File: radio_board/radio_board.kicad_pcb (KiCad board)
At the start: 2 copper layers, 82 x 72.7 mm, 86 parts, among them CN1 HX JN1.27-2X5P ZZ H4.9, Q1 2N7002K, SW2 RKB2SJG250SMTRLFS, SW3 MSK12C02, U1 FSC-BT1036C, U2 TP4057, U3 XB5352A, U4 SKB369, U5 S2B-PH-K-S(LF)(SN), U6 XC6206P332MR

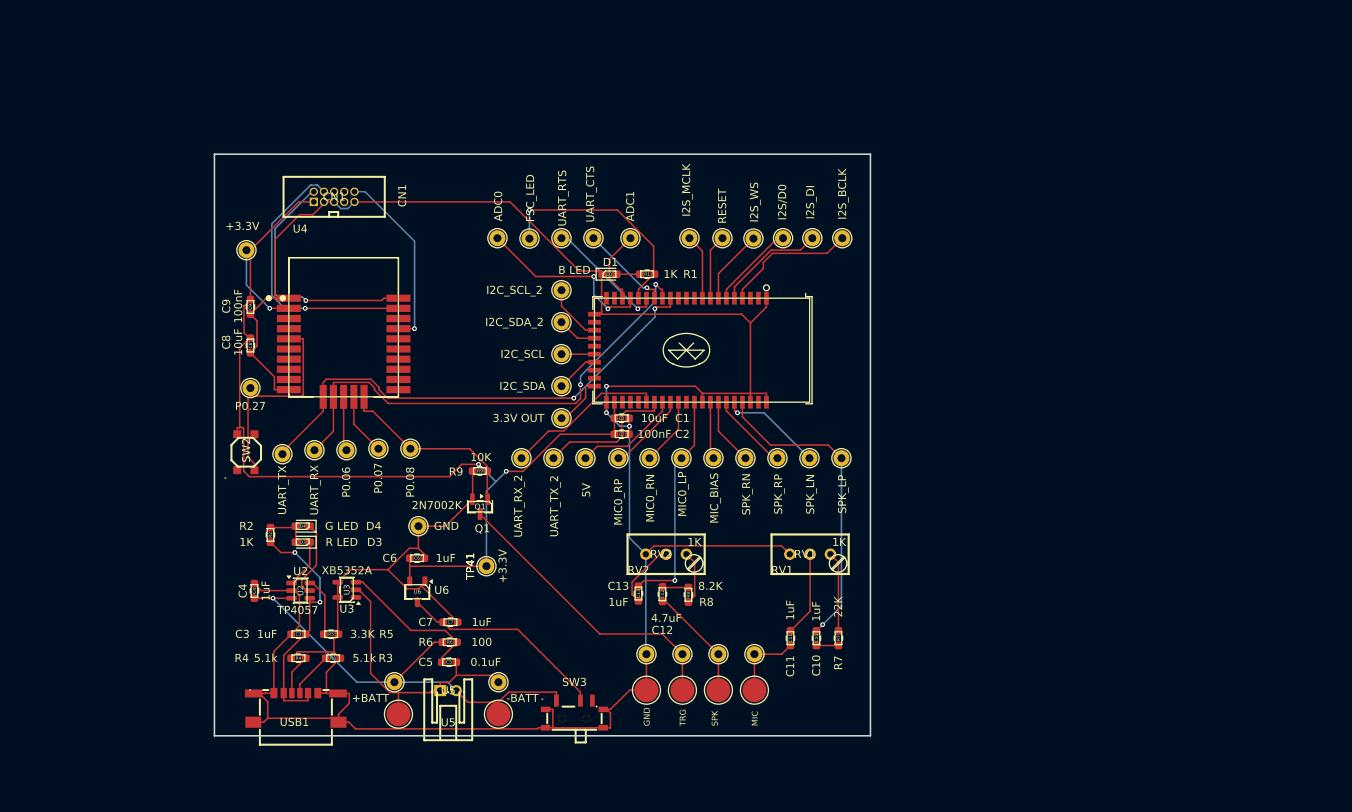
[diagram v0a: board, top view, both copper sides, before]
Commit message: [Housekeeping] Renamed project library
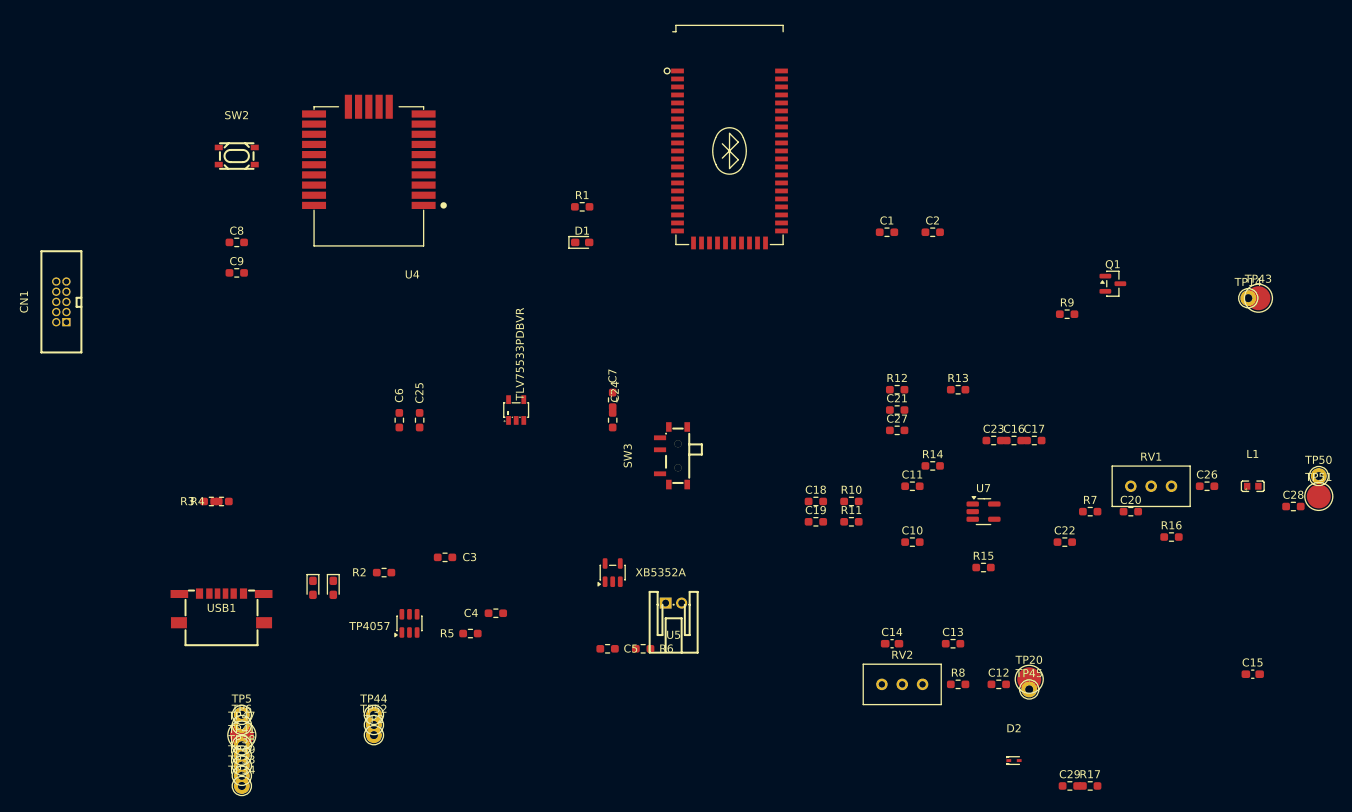
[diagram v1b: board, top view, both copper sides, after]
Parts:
- removed TP1: P0.06, TestPoint:TestPoint_THTPad_D2.0mm_Drill1.0mm
- removed TP10: UART_RX, TestPoint:TestPoint_THTPad_D2.0mm_Drill1.0mm
- removed TP11: UART_RX_2, TestPoint:TestPoint_THTPad_D2.0mm_Drill1.0mm
- removed TP12: UART_TX_2, TestPoint:TestPoint_THTPad_D2.0mm_Drill1.0mm
- removed TP13: MIC_BIAS, TestPoint:TestPoint_THTPad_D2.0mm_Drill1.0mm
- removed TP15: I2C_SCL_2, TestPoint:TestPoint_THTPad_D2.0mm_Drill1.0mm
- removed TP16: I2C_SDA_2, TestPoint:TestPoint_THTPad_D2.0mm_Drill1.0mm
- removed TP17: UART_CTS, TestPoint:TestPoint_THTPad_D2.0mm_Drill1.0mm
- removed TP18: UART_RTS, TestPoint:TestPoint_THTPad_D2.0mm_Drill1.0mm
- removed TP19: FSC_LED, TestPoint:TestPoint_THTPad_D2.0mm_Drill1.0mm
- removed TP21: 5V, TestPoint:TestPoint_THTPad_D2.0mm_Drill1.0mm
- removed TP22: RESET, TestPoint:TestPoint_THTPad_D2.0mm_Drill1.0mm
- removed TP23: I2S_WS, TestPoint:TestPoint_THTPad_D2.0mm_Drill1.0mm
- removed TP24: I2S/D0, TestPoint:TestPoint_THTPad_D2.0mm_Drill1.0mm
- removed TP25: I2S_DI, TestPoint:TestPoint_THTPad_D2.0mm_Drill1.0mm
- removed TP26: I2S_BCLK, TestPoint:TestPoint_THTPad_D2.0mm_Drill1.0mm
- removed TP27: I2S_MCLK, TestPoint:TestPoint_THTPad_D2.0mm_Drill1.0mm
- removed TP28: ADC0, TestPoint:TestPoint_THTPad_D2.0mm_Drill1.0mm
- removed TP29: ADC1, TestPoint:TestPoint_THTPad_D2.0mm_Drill1.0mm
- removed TP3: P0.08, TestPoint:TestPoint_THTPad_D2.0mm_Drill1.0mm
- removed TP30: I2C_SCL, TestPoint:TestPoint_THTPad_D2.0mm_Drill1.0mm
- removed TP31: I2C_SDA, TestPoint:TestPoint_THTPad_D2.0mm_Drill1.0mm
- removed TP32: 3.3V OUT, TestPoint:TestPoint_THTPad_D2.0mm_Drill1.0mm
- removed TP35: SPK_RP, TestPoint:TestPoint_THTPad_D2.0mm_Drill1.0mm
- removed TP36: SPK_RN, TestPoint:TestPoint_THTPad_D2.0mm_Drill1.0mm
- removed TP37: K_CONNECTOR_MIC_IN, TestPoint:TestPoint_Pad_D3.0mm
- removed TP39: MIC0_RN, TestPoint:TestPoint_THTPad_D2.0mm_Drill1.0mm
- removed TP4: P0.27, TestPoint:TestPoint_THTPad_D2.0mm_Drill1.0mm
- removed TP40: MIC0_RP, TestPoint:TestPoint_THTPad_D2.0mm_Drill1.0mm
- removed TP42: GND, TestPoint:TestPoint_THTPad_D2.0mm_Drill1.0mm
- removed TP46: GND, TestPoint:TestPoint_Pad_D3.0mm
- removed TP48: -BATT, TestPoint:TestPoint_Pad_D3.0mm
- removed TP7: +3.3V, TestPoint:TestPoint_THTPad_D2.0mm_Drill1.0mm
- removed TP8: +BATT, TestPoint:TestPoint_THTPad_D2.0mm_Drill1.0mm
- removed TP9: UART_TX, TestPoint:TestPoint_THTPad_D2.0mm_Drill1.0mm
- added C14: 1nF, Capacitor_SMD:C_0603_1608Metric_Pad1.08x0.95mm_HandSolder, F.Cu at (155.2, 117.2)
- added C15: 1uF, Capacitor_SMD:C_0603_1608Metric_Pad1.08x0.95mm_HandSolder, F.Cu at (200.3, 121.0)
- added C16: 100 nF, Resistor_SMD:R_0603_1608Metric_Pad0.98x0.95mm_HandSolder, F.Cu at (170.4, 91.8)
- added C17: 10uF, Resistor_SMD:R_0603_1608Metric_Pad0.98x0.95mm_HandSolder, F.Cu at (173.0, 91.8)
- added C18: 1uF, Resistor_SMD:R_0603_1608Metric_Pad0.98x0.95mm_HandSolder, F.Cu at (145.7, 99.4)
- added C19: 1uF, Resistor_SMD:R_0603_1608Metric_Pad0.98x0.95mm_HandSolder, F.Cu at (145.7, 102.0)
- added C20: 1uF, Resistor_SMD:R_0603_1608Metric_Pad0.98x0.95mm_HandSolder, F.Cu at (185.1, 100.7)
- added C21: 10uF, Resistor_SMD:R_0603_1608Metric_Pad0.98x0.95mm_HandSolder, F.Cu at (155.8, 88.0)
- added C22: 33 pF, Resistor_SMD:R_0603_1608Metric_Pad0.98x0.95mm_HandSolder, F.Cu at (176.8, 104.5)
- added C23: 33 pF, Resistor_SMD:R_0603_1608Metric_Pad0.98x0.95mm_HandSolder, F.Cu at (167.9, 91.8)
- added C24: 100nF, Resistor_SMD:R_0603_1608Metric_Pad0.98x0.95mm_HandSolder, F.Cu at (120.3, 89.2)
- added C25: 100nF, Resistor_SMD:R_0603_1608Metric_Pad0.98x0.95mm_HandSolder, F.Cu at (96.2, 89.2)
- added C26: 1uF, Resistor_SMD:R_0603_1608Metric_Pad0.98x0.95mm_HandSolder, F.Cu at (194.6, 97.5)
- added C27: 100nF, Resistor_SMD:R_0603_1608Metric_Pad0.98x0.95mm_HandSolder, F.Cu at (155.8, 90.5)
- added C28: 1nF, Resistor_SMD:R_0603_1608Metric_Pad0.98x0.95mm_HandSolder, F.Cu at (205.4, 100.0)
- added C29: 100nF, Resistor_SMD:R_0603_1608Metric_Pad0.98x0.95mm_HandSolder, F.Cu at (177.4, 135.0)
- added D2: RB521S-30_C727120, PTT_Project_library:SOD-523_L1.2-W0.8-LS1.6-RD, F.Cu at (170.4, 131.8)
- added L1: BLM18KG601SN1D, PTT_Project_library:L0603, F.Cu at (200.3, 97.5)
- added R10: 47k, Resistor_SMD:R_0603_1608Metric_Pad0.98x0.95mm_HandSolder, F.Cu at (150.1, 99.4)
- added R11: 47k, Resistor_SMD:R_0603_1608Metric_Pad0.98x0.95mm_HandSolder, F.Cu at (150.1, 102.0)
- added R12: 10k, Resistor_SMD:R_0603_1608Metric_Pad0.98x0.95mm_HandSolder, F.Cu at (155.8, 85.4)
- added R13: 10k, Resistor_SMD:R_0603_1608Metric_Pad0.98x0.95mm_HandSolder, F.Cu at (163.5, 85.4)
- added R14: 10k, Resistor_SMD:R_0603_1608Metric_Pad0.98x0.95mm_HandSolder, F.Cu at (160.3, 95.0)
- added R15: 10k, Resistor_SMD:R_0603_1608Metric_Pad0.98x0.95mm_HandSolder, F.Cu at (166.6, 107.7)
- added R16: 100, Resistor_SMD:R_0603_1608Metric_Pad0.98x0.95mm_HandSolder, F.Cu at (190.1, 103.9)
- added R17: 470k, Resistor_SMD:R_0603_1608Metric_Pad0.98x0.95mm_HandSolder, F.Cu at (180.0, 135.0)
- added TP49: MIC0_LN, TestPoint:TestPoint_THTPad_D2.0mm_Drill1.0mm, F.Cu at (73.9, 132.4)
- added TP50: K_CONNECTOR_MIC_IN, TestPoint:TestPoint_THTPad_D2.0mm_Drill1.0mm, F.Cu at (208.5, 96.2)
- added TP51: K_CONNECTOR_MIC_IN, TestPoint:TestPoint_Pad_D3.0mm, F.Cu at (208.5, 98.8)
- added TP52: P0.31, TestPoint:TestPoint_THTPad_D2.0mm_Drill1.0mm, F.Cu at (90.4, 127.3)
- added U7: LMV321, Package_TO_SOT_SMD:SOT-23-5_HandSoldering, F.Cu at (166.6, 100.7)
- C10, C11: value 1uF -> 33 pF
- C6, C7: value 1uF -> 10uF
- CN1: footprint PTT_project:CONN-TH_10P-P1.27_HX-JN1.27-2X5P-ZZ-H4.9 -> PTT_Project_library:CONN-TH_10P-P1.27_HX-JN1.27-2X5P-ZZ-H4.9
- R7: value 22K -> 4.7k
- SW2: footprint PTT_project:Push button C2927788 -> PTT_Project_library:SW-SMD_4P-L4.2-W3.2-P2.15-LS4.6
- SW3: footprint PTT_project:SW-TH_MSK12C02 -> PTT_Project_library:SW-TH_MSK12C02
- TP2: value P0.07 -> P0.08
- TP44: value K_CONNECTOR_MIC_IN -> P0.30
- U1: footprint PTT_project:FSC-BT1036C -> PTT_Project_library:FSC-BT1036C
- U4: footprint PTT_project:SKYLAB_SKB369 -> PTT_Project_library:SKYLAB_SKB369
- U5: footprint PTT_project:CONN-TH_S2B-PH-K-S-LF-SN -> PTT_Project_library:CONN-TH_S2B-PH-K-S-LF-SN
- U6: value XC6206P332MR -> TLV75533PDBVR; footprint Package_TO_SOT_SMD:TSOT-23 -> PTT_Project_library:SOT-23-5_L3.0-W1.7-P0.95-LS2.8-BR
- USB1: footprint PTT_project:USB-C-SMD_TYPE-C-6P-QT073 -> PTT_Project_library:USB-C-SMD_TYPE-C-6P-QT073
- moved TP43 87.1 mm to (201.0, 74.0), turned to 0 degrees
- moved TP33 84.8 mm to (73.9, 133.7), turned to 0 degrees
- moved Q1 83.9 mm to (182.8, 72.2), turned to 0 degrees
- moved TP14 83.6 mm to (199.7, 74.0)
- moved TP34 81.9 mm to (73.9, 135.0), turned to 0 degrees
- moved R9 76.0 mm to (177.1, 76.0), turned to 0 degrees
- moved TP38 66.3 mm to (73.9, 131.2), turned to 0 degrees
- moved TP5 51.1 mm to (73.9, 126.1), turned to 0 degrees
- moved TP44 48.2 mm to (90.4, 126.1)
- moved C2 46.4 mm to (160.3, 65.8), turned to 0 degrees
- moved C12 43.5 mm to (168.5, 122.3), turned to 0 degrees
- moved RV1 43.5 mm to (190.1, 97.5)
- moved C1 40.5 mm to (154.6, 65.8), turned to 0 degrees
- moved C13 39.8 mm to (162.8, 117.2), turned to 0 degrees
- moved TP45 39.1 mm to (172.3, 122.9)
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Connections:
- C1 pad 1: GND -> +3.3V
- C10 pad 1: SPK_LP -> Net-(U7--)
- C10 pad 2: Net-(C10-Pad2) -> +3.3V
- C11 pad 1: Net-(C11-Pad1) -> Net-(U7-+)
- C11 pad 2: Net-(C11-Pad2) -> +3.3V
- C13 pad 1: MIC0_LP -> Net-(C13-Pad1)
- C13 pad 2: Net-(C13-Pad2) -> MIC0_LP
- C2 pad 1: GND -> +3.3V
- C3 pad 1: GND -> +3.3V
- C4 pad 2: GND -> +3.3V
- C6 pad 2: GND -> +3.3V
- C7 pad 1: GND -> +3.3V
- C7 pad 2: Net-(U6-VIN) -> Net-(U6-EN)
- C8 pad 1: GND -> +3.3V
- C9 pad 1: GND -> +3.3V
- CN1 pad 3: GND -> +3.3V
- CN1 pad 5: GND -> +3.3V
- CN1 pad 9: GND -> +3.3V
- D1 pad 1: GND -> +3.3V
- Q1 pad 2: GND -> +3.3V
- R3 pad 1: GND -> +3.3V
- R4 pad 1: GND -> +3.3V
- R5 pad 2: GND -> +3.3V
- R7 pad 1: Net-(C10-Pad2) -> Net-(C22-Pad2)
- R7 pad 2: Net-(R7-Pad2) -> Net-(C20-Pad1)
- R9 pad 2: GND -> +3.3V
- RV1 pad 1: Net-(R7-Pad2) -> unconnected-(RV1-Pad1)
- RV1 pad 2: Net-(C11-Pad2) -> Net-(C26-Pad1)
- RV1 pad 3: GND -> Net-(C20-Pad2)
- RV2 pad 2: Net-(C13-Pad2) -> Net-(C13-Pad1)
- RV2 pad 3: GND -> +3.3V
- SW3 pad 2: Net-(U6-VIN) -> unconnected-(SW3-Pad2)
- SW3 pad 4: GND -> +3.3V
- TP2 pad 1: Net-(U4-P0.07) -> P0.08
- TP44 pad 1: Net-(C11-Pad1) -> P0.30
- TP5 pad 1: GND -> +3.3V
- U1 pad 1: GND -> +3.3V
- U1 pad 15: Net-(U1-P4/UART_CTS) -> unconnected-(U1-P4/UART_CTS-Pad15)
- U1 pad 16: Net-(U1-P5/UART_RTS) -> unconnected-(U1-P5/UART_RTS-Pad16)
- U1 pad 18: Net-(U1-P11/ADC0) -> unconnected-(U1-P11/ADC0-Pad18)
- U1 pad 19: Net-(TP29-Pad1) -> unconnected-(U1-P37/ADC1-Pad19)
- U1 pad 22: GND -> +3.3V
- U1 pad 24: Net-(TP15-Pad1) -> unconnected-(U1-P38/I2C_SCL-Pad24)
- U1 pad 25: Net-(TP16-Pad1) -> unconnected-(U1-P39/I2C_SDA-Pad25)
- U1 pad 27: Net-(TP30-Pad1) -> unconnected-(U1-P38/I2C_SCL-Pad27)
- U1 pad 28: Net-(TP31-Pad1) -> unconnected-(U1-P39/I2C_SDA-Pad28)
- U1 pad 31: Net-(U1-3.3V_OUT) -> unconnected-(U1-3.3V_OUT-Pad31)
- U1 pad 32: GND -> +3.3V
- U1 pad 37: Net-(TP11-Pad1) -> unconnected-(U1-P1/UART_RX/DP-Pad37)
- U1 pad 38: Net-(TP12-Pad1) -> unconnected-(U1-P0/UART_TX/DN-Pad38)
- U1 pad 39: Net-(U1-+5V) -> unconnected-(U1-+5V-Pad39)
- U1 pad 4: Net-(U1-P30/I2S_BCLK) -> unconnected-(U1-P30/I2S_BCLK-Pad4)
- U1 pad 44: GND -> MIC0_LN
- U1 pad 5: Net-(U1-P32/I2S_DI) -> unconnected-(U1-P32/I2S_DI-Pad5)
- U1 pad 50: GND -> +3.3V
- U1 pad 52: GND -> +3.3V
- U1 pad 6: Net-(U1-P33//I2S_DO) -> unconnected-(U1-P33//I2S_DO-Pad6)
- U1 pad 7: Net-(U1-P31/I2S_WS) -> unconnected-(U1-P31/I2S_WS-Pad7)
- U1 pad 8: Net-(U1-RESET) -> RESET_FSC
- U1 pad 9: Net-(U1-I2S_MCLK) -> unconnected-(U1-I2S_MCLK-Pad9)
- U2 pad 2: GND -> +3.3V
- U3 pad 4: GND -> +3.3V
- U3 pad 5: GND -> +3.3V
- U4 pad 1: GND -> +3.3V
- U4 pad 10: GND -> +3.3V
- U4 pad 13: Net-(U4-P0.06) -> unconnected-(U4-P0.06-Pad13)
- U4 pad 14: Net-(U4-P0.07) -> unconnected-(U4-P0.07-Pad14)
- U4 pad 22: RESET -> RESET_SKB
- U4 pad 8: unconnected-(U4-P0.30-Pad8) -> P0.30
- U4 pad 9: unconnected-(U4-P0.31-Pad9) -> P0.31
- U6 pad 1: GND -> Net-(U6-EN)
- U6 pad 3: Net-(U6-VIN) -> Net-(U6-EN)
- USB1 pad 7: GND -> +3.3V
- USB1 pad A12: GND -> +3.3V
- USB1 pad B12: GND -> +3.3V
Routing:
- net GND: track 350.4 -> 0.00 mm, vias 3 -> 0
- net +3.3V: track 130.3 -> 0.00 mm, vias 3 -> 0
- net UART_TX: track 62.2 -> 0.00 mm, vias 2 -> 0
- net UART_RX: track 62.2 -> 0.00 mm, vias 2 -> 0
- net +BATT: track 56.6 -> 0.00 mm, vias 1 -> 0
- net SPK_LP: track 39.2 -> 0.00 mm, vias 1 -> 0
- net Net-(Q1-D): track 37.0 -> 0.00 mm
- net -BATT: track 34.6 -> 0.00 mm
- net SWDCLK: track 34.3 -> 0.00 mm, vias 1 -> 0
- net SWDIO: track 30.8 -> 0.00 mm, vias 1 -> 0
- net 5V_usb: track 30.6 -> 0.00 mm, vias 2 -> 0
- net FSC_LED: track 28.4 -> 0.00 mm, vias 1 -> 0
- net MIC0_LP: track 28.2 -> 0.00 mm, vias 1 -> 0
- net Net-(U4-P0.27): track 26.2 -> 0.00 mm
- net Net-(U6-VIN): track 26.1 -> 0.00 mm
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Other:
- board outline removed
- board text removed: "GND"
- board text removed: "MIC"
- board text removed: "SPK"
- board text removed: "TRG"

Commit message: [WIP]
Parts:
- removed U4: SKB369, PTT_Project_library:SKYLAB_SKB369
- added C30: 100nF, Resistor_SMD:R_0603_1608Metric_Pad0.98x0.95mm_HandSolder, F.Cu at (70.8, 60.2)
- added C31: 100nF, Resistor_SMD:R_0603_1608Metric_Pad0.98x0.95mm_HandSolder, F.Cu at (123.0, 47.5)
- added D5: B LED, LED_SMD:LED_0603_1608Metric_Pad1.05x0.95mm_HandSolder, F.Cu at (73.9, 71.0)
- added R18: 10K, Resistor_SMD:R_0603_1608Metric_Pad0.98x0.95mm_HandSolder, F.Cu at (93.0, 54.0)
- added R19: 1K, Resistor_SMD:R_0603_1608Metric_Pad0.98x0.95mm_HandSolder, F.Cu at (73.9, 66.5)
- added R20: 10K, Resistor_SMD:R_0603_1608Metric_Pad0.98x0.95mm_HandSolder, F.Cu at (123.0, 50.0)
- added U8: STM32G030F6P6TR, PTT_Project_library:TSSOP-20_L6.5-W4.4-P0.65-LS6.4-BL, F.Cu at (83.9, 57.1)
- TP2: value P0.08 -> PTT_Trigger
- TP44: value P0.30 -> Squelch_detect
- TP52: value P0.31 -> Debug_gpio
- moved CN1 145.1 mm to (196.5, 72.3), turned to 0 degrees
- moved TP14 27.8 mm to (197.8, 46.2)
- moved TP43 27.8 mm to (199.0, 46.2)
- moved Q1 26.0 mm to (196.5, 50.0)
- moved R9 26.0 mm to (190.8, 53.9)
- moved C9 17.3 mm to (77.1, 54.0)
- moved C8 16.0 mm to (77.1, 51.5)
- moved SW2 14.6 mm to (86.0, 49.0)
- moved C1 8.96 mm to (163.5, 64.6)
- moved C2 8.96 mm to (169.2, 64.6)
- moved U1 8.96 mm to (143.8, 54.5)
- moved D1 8.96 mm to (125.4, 65.9)
- moved R1 8.96 mm to (125.4, 61.5)
- moved C20 2.20 mm to (183.2, 99.6)
- moved R7 2.20 mm to (178.1, 99.6)
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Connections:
- net P0.08 renamed PTT_Trigger
- net P0.30 renamed Squelch_detect
- C1 pad 1: +3.3V -> GND
- C10 pad 2: +3.3V -> GND
- C11 pad 2: +3.3V -> GND
- C14 pad 1: +3.3V -> GND
- C15 pad 1: +3.3V -> GND
- C16 pad 1: +3.3V -> GND
- C17 pad 1: +3.3V -> GND
- C2 pad 1: +3.3V -> GND
- C21 pad 1: +3.3V -> GND
- C22 pad 1: +3.3V -> GND
- C23 pad 1: +3.3V -> GND
- C24 pad 1: +3.3V -> Net-(C24-Pad1)
- C25 pad 1: +3.3V -> GND
- C27 pad 1: +3.3V -> GND
- C28 pad 2: +3.3V -> GND
- C29 pad 2: +3.3V -> GND
- C3 pad 1: +3.3V -> GND
- C4 pad 2: +3.3V -> GND
- C6 pad 1: +3.3V -> GND
- C7 pad 1: +3.3V -> Net-(C24-Pad1)
- C8 pad 1: +3.3V -> GND
- C9 pad 1: +3.3V -> GND
- CN1 pad 3: +3.3V -> GND
- CN1 pad 5: +3.3V -> GND
- CN1 pad 9: +3.3V -> GND
- D1 pad 1: +3.3V -> GND
- Q1 pad 2: +3.3V -> GND
- R12 pad 1: +3.3V -> GND
- R16 pad 2: +3.3V -> GND
- R17 pad 1: +3.3V -> GND
- R3 pad 1: +3.3V -> GND
- R4 pad 1: +3.3V -> GND
- R5 pad 2: +3.3V -> GND
- R9 pad 2: +3.3V -> GND
- RV2 pad 3: +3.3V -> GND
- SW3 pad 2: unconnected-(SW3-Pad2) -> Net-(C24-Pad1)
- SW3 pad 4: +3.3V -> GND
- TP5 pad 1: +3.3V -> GND
- TP52 pad 1: P0.31 -> Debug_gpio
- U1 pad 1: +3.3V -> GND
- U1 pad 22: +3.3V -> GND
- U1 pad 32: +3.3V -> GND
- U1 pad 50: +3.3V -> GND
- U1 pad 52: +3.3V -> GND
- U2 pad 2: +3.3V -> GND
- U3 pad 4: +3.3V -> GND
- U3 pad 5: +3.3V -> GND
- U6 pad 2: +3.3V -> GND
- U7 pad 2: +3.3V -> GND
- USB1 pad 7: +3.3V -> GND
- USB1 pad A12: +3.3V -> GND
- USB1 pad B12: +3.3V -> GND

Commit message: [WIP]
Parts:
- removed C31: 100nF, Resistor_SMD:R_0603_1608Metric_Pad0.98x0.95mm_HandSolder
- removed R20: 10K, Resistor_SMD:R_0603_1608Metric_Pad0.98x0.95mm_HandSolder
- removed TP2: PTT_Trigger, TestPoint:TestPoint_THTPad_D2.0mm_Drill1.0mm
- removed TP33: SPK_LP, TestPoint:TestPoint_THTPad_D2.0mm_Drill1.0mm
- removed TP34: SPK_LN, TestPoint:TestPoint_THTPad_D2.0mm_Drill1.0mm
- removed TP38: MIC0_LP, TestPoint:TestPoint_THTPad_D2.0mm_Drill1.0mm
- removed TP41: +3.3V, TestPoint:TestPoint_THTPad_D2.0mm_Drill1.0mm
- removed TP44: Squelch_detect, TestPoint:TestPoint_THTPad_D2.0mm_Drill1.0mm
- removed TP47: +BATT, TestPoint:TestPoint_Pad_D3.0mm
- removed TP49: MIC0_LN, TestPoint:TestPoint_THTPad_D2.0mm_Drill1.0mm
- removed TP5: GND, TestPoint:TestPoint_THTPad_D2.0mm_Drill1.0mm
- removed TP52: Debug_gpio, TestPoint:TestPoint_THTPad_D2.0mm_Drill1.0mm
- removed TP6: -BATT, TestPoint:TestPoint_THTPad_D2.0mm_Drill1.0mm
- added R21: 150K, Resistor_SMD:R_0603_1608Metric_Pad0.98x0.95mm_HandSolder, F.Cu at (114.5, 89.8)
- added R22: 100K, Resistor_SMD:R_0603_1608Metric_Pad0.98x0.95mm_HandSolder, F.Cu at (112.2, 89.8)
- added R23: Poka Yoke UART, poka_yuke:poka_yoke_uart_Solder, F.Cu at (111.3, 69.4)
- moved R17 81.8 mm to (114.0, 83.0), turned to 180 degrees
- moved C29 81.4 mm to (113.8, 80.8)
- moved C15 79.6 mm to (140.2, 65.5), turned to 180 degrees
- moved TP43 77.7 mm to (137.0, 93.0)
- moved Q1 74.6 mm to (131.4, 86.7), turned to -90 degrees
- moved R9 74.5 mm to (123.8, 86.5)
- moved TP14 73.7 mm to (140.8, 93.0)
- moved CN1 71.2 mm to (128.0, 91.6), turned to 180 degrees
- moved C30 62.5 mm to (130.4, 78.8)
- moved C8 62.4 mm to (131.6, 81.8), turned to -90 degrees
- moved C9 59.3 mm to (129.4, 81.9), turned to -90 degrees
- moved R5 58.1 mm to (112.2, 57.9), turned to -90 degrees
- moved USB1 57.4 mm to (98.9, 62.3), turned to -90 degrees
- moved TP50 56.8 mm to (155.2, 71.0), turned to -90 degrees
- moved D4 56.6 mm to (112.2, 61.9), turned to 90 degrees
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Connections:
- R16 pad 1: Net-(C20-Pad2) -> GND
- R16 pad 2: GND -> Net-(C20-Pad2)
- U1 pad 8: RESET_FSC -> unconnected-(U1-RESET-Pad8)
- U8 pad 1: UART_TX -> Net-(U8-PB7/PB8)
- U8 pad 12: +BATT -> Net-(U8-PA5)
- U8 pad 20: UART_RX -> Net-(U8-PB3/PB4/PB5/PB6)
- U8 pad 9: RESET_FSC -> unconnected-(U8-PA2-Pad9)
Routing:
- net +3.3V: track 0.00 -> 64.7 mm
- net +BATT: track 0.00 -> 40.9 mm
- net Squelch_detect: track 0.00 -> 30.4 mm
- net SWDIO: track 0.00 -> 29.2 mm
- net RESET: track 0.00 -> 23.9 mm
- net Net-(U8-PB7/PB8): track 0.00 -> 19.4 mm
- net Net-(U8-PA4): track 0.00 -> 15.6 mm
- net (no net): track 0.00 -> 12.9 mm
- net Net-(U8-PB3/PB4/PB5/PB6): track 0.00 -> 12.6 mm
- added copper zone on B.Cu, net GND
- added copper zone on F.Cu, net GND
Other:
- board outline added: 63.4 x 46.8 mm

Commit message: [WIP]
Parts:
- removed CN1: HX JN1.27-2X5P ZZ H4.9, PTT_Project_library:CONN-TH_10P-P1.27_HX-JN1.27-2X5P-ZZ-H4.9
- added J1: 3.3v, Connector_PinSocket_2.54mm:PinSocket_1x01_P2.54mm_Vertical, F.Cu at (77.8, 79.5)
- added J2: GND, Connector_PinSocket_2.54mm:PinSocket_1x01_P2.54mm_Vertical, F.Cu at (133.0, 92.5)
- added J3: RESET, Connector_PinSocket_2.54mm:PinSocket_1x01_P2.54mm_Vertical, F.Cu at (120.9, 88.8)
- added J4: SWDCLK, Connector_PinSocket_2.54mm:PinSocket_1x01_P2.54mm_Vertical, F.Cu at (116.7, 75.2)
- added J5: SWDIO, Connector_PinSocket_2.54mm:PinSocket_1x01_P2.54mm_Vertical, F.Cu at (120.2, 75.2)
- added R20: 1, Resistor_SMD:R_0603_1608Metric_Pad0.98x0.95mm_HandSolder, F.Cu at (106.0, 78.7)
- added TP1: TP_IBATT_H, TestPoint:TestPoint_THTPad_D2.0mm_Drill1.0mm, F.Cu at (103.0, 80.2)
- added TP2: PTT_Trigger, TestPoint:TestPoint_THTPad_D2.0mm_Drill1.0mm, F.Cu at (126.1, 77.8)
- added TP3: TP_IBATT_L, TestPoint:TestPoint_THTPad_D2.0mm_Drill1.0mm, F.Cu at (79.0, 68.8)
- added TP33: SPK_LP, TestPoint:TestPoint_THTPad_D2.0mm_Drill1.0mm, F.Cu at (135.2, 51.8)
- added TP34: SPK_LN, TestPoint:TestPoint_THTPad_D2.0mm_Drill1.0mm, F.Cu at (132.0, 54.0)
- added TP38: MIC0_LP, TestPoint:TestPoint_THTPad_D2.0mm_Drill1.0mm, F.Cu at (131.7, 60.5)
- added TP41: +3.3V, TestPoint:TestPoint_THTPad_D2.0mm_Drill1.0mm, F.Cu at (139.2, 68.5)
- added TP44: Squelch_detect, TestPoint:TestPoint_THTPad_D2.0mm_Drill1.0mm, F.Cu at (129.8, 77.8)
- added TP47: +BATT, TestPoint:TestPoint_Pad_D2.5mm, F.Cu at (98.2, 80.0)
- added TP49: MIC0_LN, TestPoint:TestPoint_THTPad_D2.0mm_Drill1.0mm, F.Cu at (131.7, 57.3)
- added TP5: GND, TestPoint:TestPoint_THTPad_D2.0mm_Drill1.0mm, F.Cu at (137.2, 92.8)
- added TP6: -BATT, TestPoint:TestPoint_Pad_D2.5mm, F.Cu at (98.3, 68.6)
- moved D5 19.5 mm to (120.3, 93.6), turned to 180 degrees
- moved C8 18.4 mm to (115.1, 89.8), turned to 180 degrees
- moved R19 17.2 mm to (120.3, 91.6), turned to 0 degrees
- moved C30 16.0 mm to (118.0, 88.8), turned to -90 degrees
- moved R17 15.6 mm to (129.5, 81.5), turned to 90 degrees
- moved C9 15.5 mm to (115.1, 87.8), turned to 180 degrees
- moved R18 14.3 mm to (113.2, 75.8)
- moved C29 13.7 mm to (127.5, 81.4), turned to -90 degrees
- moved R22 13.0 mm to (125.3, 89.5), turned to 0 degrees
- moved SW2 12.0 mm to (121.8, 82.0), turned to -90 degrees
- moved C13 11.8 mm to (136.7, 59.9), turned to 90 degrees
- moved R21 11.0 mm to (125.3, 87.6), turned to 180 degrees
- moved C7 10.8 mm to (98.8, 85.3), turned to -90 degrees
- moved C6 10.6 mm to (109.0, 85.0)
- moved C14 10.3 mm to (136.7, 63.8), turned to 90 degrees
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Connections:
- R23 pad 1: UART_TX -> Net-(U8-PB7/PB8)
- R23 pad 4: Net-(U8-PB7/PB8) -> UART_TX
- SW2 pad 2: +3.3V -> GND
- SW2 pad 3: unconnected-(SW2-Pad3) -> Net-(U8-PA4)
- SW2 pad 4: Net-(U8-PA4) -> unconnected-(SW2-Pad4)
- U1 pad 45: MIC_BIAS -> unconnected-(U1-MIC_BIAS-Pad45)
- U5 pad 2: +BATT -> Net-(R20-Pad1)
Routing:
- net +BATT: track 40.9 -> 68.7 mm, vias 0 -> 2
- net PTT_Trigger: track 0.00 -> 22.6 mm
- net Net-(C13-Pad1): track 0.00 -> 21.3 mm, vias 0 -> 1
- net SWDIO: track 29.2 -> 8.81 mm
- net +3.3V: track 64.7 -> 82.3 mm, vias 0 -> 2
- net Net-(C28-Pad1): track 0.00 -> 17.4 mm
- net RESET: track 23.9 -> 6.91 mm
- net 5V_usb: track 0.00 -> 16.3 mm
- net Net-(C12-Pad1): track 0.00 -> 15.7 mm
- net UART_RX: track 0.00 -> 15.3 mm
- net UART_TX: track 0.00 -> 14.5 mm
- net Net-(Q1-D): track 0.00 -> 14.5 mm
- net Debug_gpio: track 0.00 -> 14.3 mm
- net -BATT: track 0.00 -> 14.0 mm
- net Net-(R20-Pad1): track 0.00 -> 13.8 mm
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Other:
- board size 63.4 x 46.8 mm -> 61.7 x 46.5 mm
